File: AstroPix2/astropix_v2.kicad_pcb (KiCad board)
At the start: 4 copper layers, 51.3 x 48.8 mm, 45 parts, among them J1 pcie_GECCO, J10 SPI_right, J3 Vtemp1, J4 SFOut, J5 sample_clock_out, J6 HV_in_external, J8 VBias, J9 SPI_left, U1 TLV333, U2 SN65LVDS4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

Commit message: PCB: Small corrections
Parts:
- removed J8: VBias, Connector_PinHeader_2.54mm:PinHeader_1x03_P2.54mm_Vertical
- moved C11 3.20 mm to (120.8, 96.1)
- moved C14 3.17 mm to (117.6, 96.1)
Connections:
- U4 pad B24: /VPBias -> (no net)
- U4 pad B25: /pamp -> (no net)

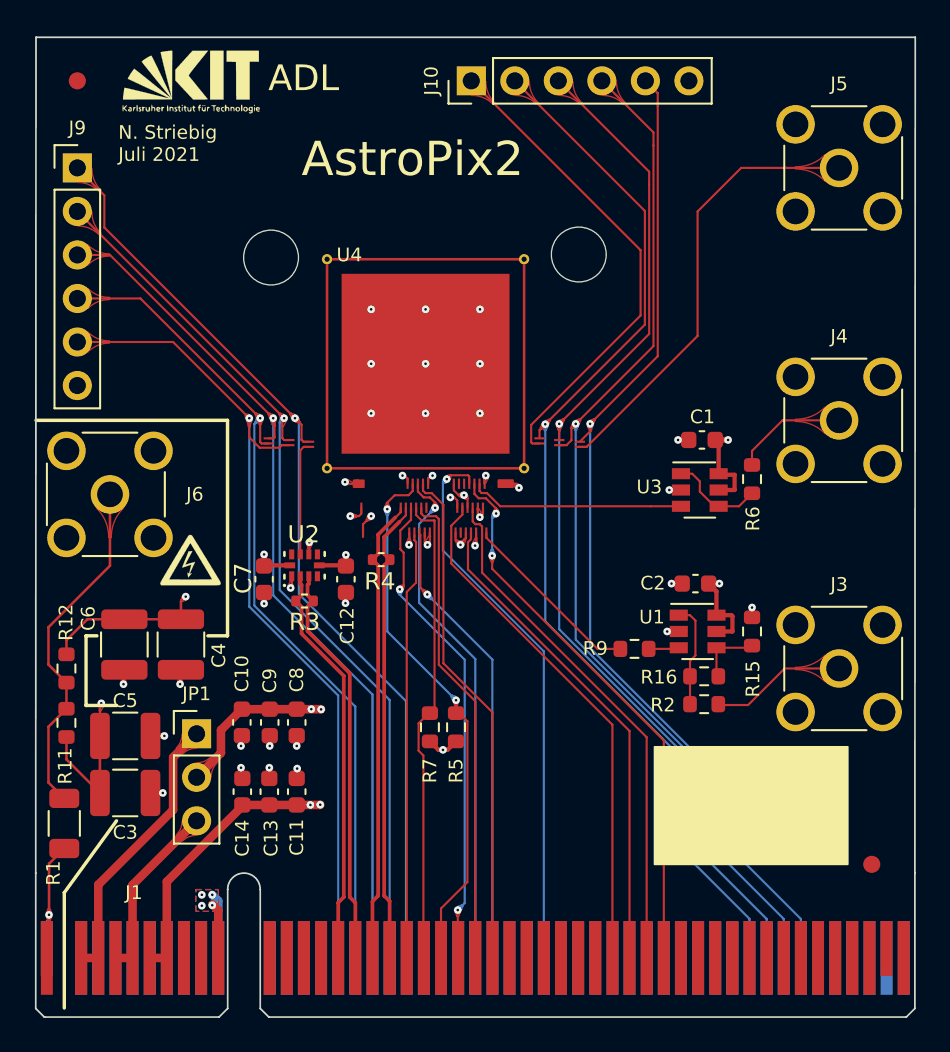
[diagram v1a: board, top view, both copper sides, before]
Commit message: PCB: Apix v2 updates
- Added SPI series resistors
- connected spi_right_clk to FMC
- Updated Amplifier Layout
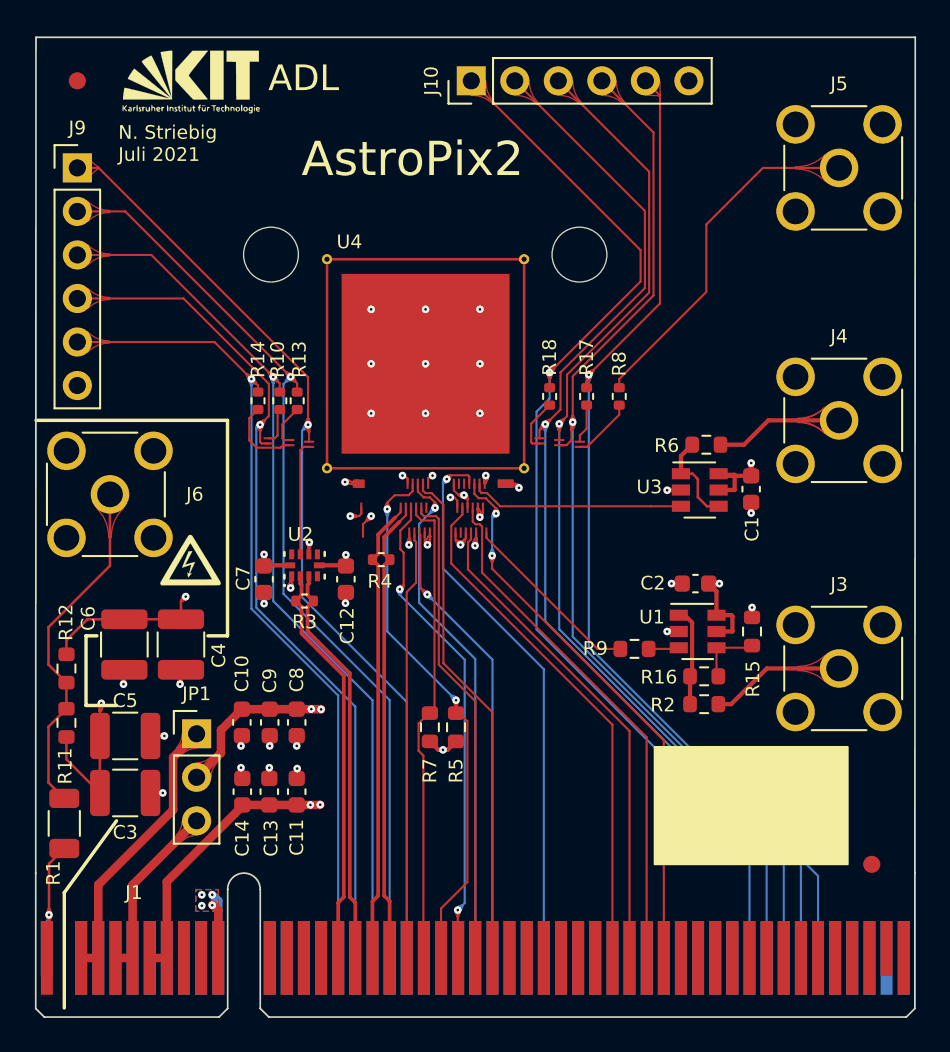
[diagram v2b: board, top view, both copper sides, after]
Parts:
- added R10: 22, Resistor_SMD:R_0402_1005Metric, F.Cu at (119.8, 73.3)
- added R13: 22, Resistor_SMD:R_0402_1005Metric, F.Cu at (120.8, 73.3)
- added R14: 22, Resistor_SMD:R_0402_1005Metric, F.Cu at (118.5, 73.3)
- added R17: 22, Resistor_SMD:R_0402_1005Metric, F.Cu at (137.7, 73.0)
- added R18: 22, Resistor_SMD:R_0402_1005Metric, F.Cu at (135.5, 73.0)
- added R8: 22, Resistor_SMD:R_0402_1005Metric, F.Cu at (139.6, 73.0)
- R6: value 22 -> 47
- moved C1 4.06 mm to (147.3, 78.4), turned to 270 degrees
- moved R6 3.34 mm to (144.7, 75.8), turned to 180 degrees
- moved H1 0.17 mm to (119.2, 64.8)
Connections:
- J1 pad A40: /spi_right_miso1 -> /spi_right_clk
- J1 pad A41: /spi_right_miso0 -> /spi_right_miso1
- J1 pad A42: /spi_right_csn -> /spi_right_miso0
- J1 pad A43: /spi_right_mosi -> /spi_right_csn
- J1 pad A44: (no net) -> /spi_right_mosi
- U4 pad L1: /spi_left_miso1 -> Net-(R10-Pad1)
- U4 pad L2: /spi_left_miso0 -> Net-(R13-Pad1)
- U4 pad L5: /spi_left_csn -> Net-(R14-Pad1)
- U4 pad R1: /sc_out -> Net-(R8-Pad2)
- U4 pad R3: /spi_right_clk -> Net-(R18-Pad2)
- U4 pad R4: /spi_right_mosi -> Net-(R17-Pad2)
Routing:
- net /spi_right_clk: track 28.3 -> 63.8 mm, vias 0 -> 1
- net /sc_out: track 26.2 -> 20.7 mm
- net Net-(R14-Pad1): track 0.00 -> 4.59 mm
- net Net-(J4-Pad1): track 6.64 -> 10.8 mm
- net Net-(R8-Pad2): track 0.00 -> 3.64 mm
- net Net-(R18-Pad2): track 0.00 -> 3.13 mm
- net Net-(R13-Pad1): track 0.00 -> 2.48 mm
- net Net-(R17-Pad2): track 0.00 -> 2.30 mm
- net Net-(R10-Pad1): track 0.00 -> 2.15 mm
- net /spi_left_csn: track 49.5 -> 47.9 mm
- net /spi_left_clk: track 49.6 -> 51.0 mm
- net /spi_left_miso0: track 53.0 -> 54.1 mm
- net /spi_left_miso1: track 50.8 -> 51.7 mm
- net /spi_right_csn: track 61.2 -> 61.8 mm

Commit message: PCB: Added holes for HIT bonding fixture
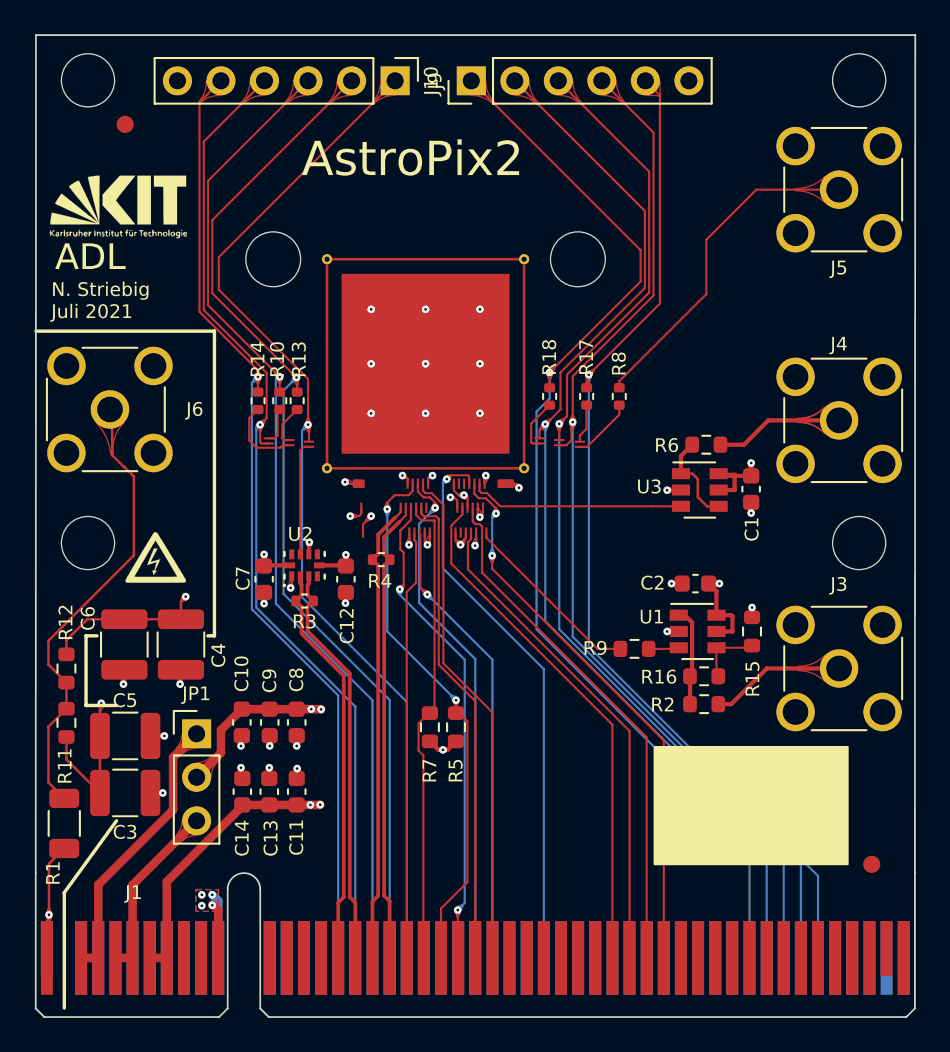
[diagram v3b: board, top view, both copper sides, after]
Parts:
- added H3: bonder, astropix:bonder, F.Cu at (131.6, 68.6)
- moved J9 19.2 mm to (126.5, 54.6), turned to 270 degrees
- moved Logo1 8.43 mm to (110.4, 62.0)
- moved J6 4.95 mm to (109.9, 73.8)
- moved FID1 3.78 mm to (110.7, 57.1)
- moved Logo2 2.04 mm to (112.5, 82.4)
- moved J5 1.27 mm to (152.4, 61.0)
- moved H1 0.30 mm to (119.4, 65.0)
- moved H2 0.29 mm to (137.2, 65.0)
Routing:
- net /spi_left_csn: track 47.9 -> 56.2 mm
- net /spi_left_clk: track 51.0 -> 58.4 mm
- net /spi_left_miso1: track 51.7 -> 58.6 mm
- net /spi_left_miso0: track 54.1 -> 60.3 mm
- net /HV_in_ext: track 20.5 -> 26.6 mm
- net /spi_left_mosi: track 56.1 -> 61.3 mm
- net /sc_out: track 20.7 -> 19.7 mm
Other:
- board size 51.3 x 48.8 mm -> 51.3 x 48.9 mm

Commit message: PCB V2: Connected SR_out/RB + Updated production files
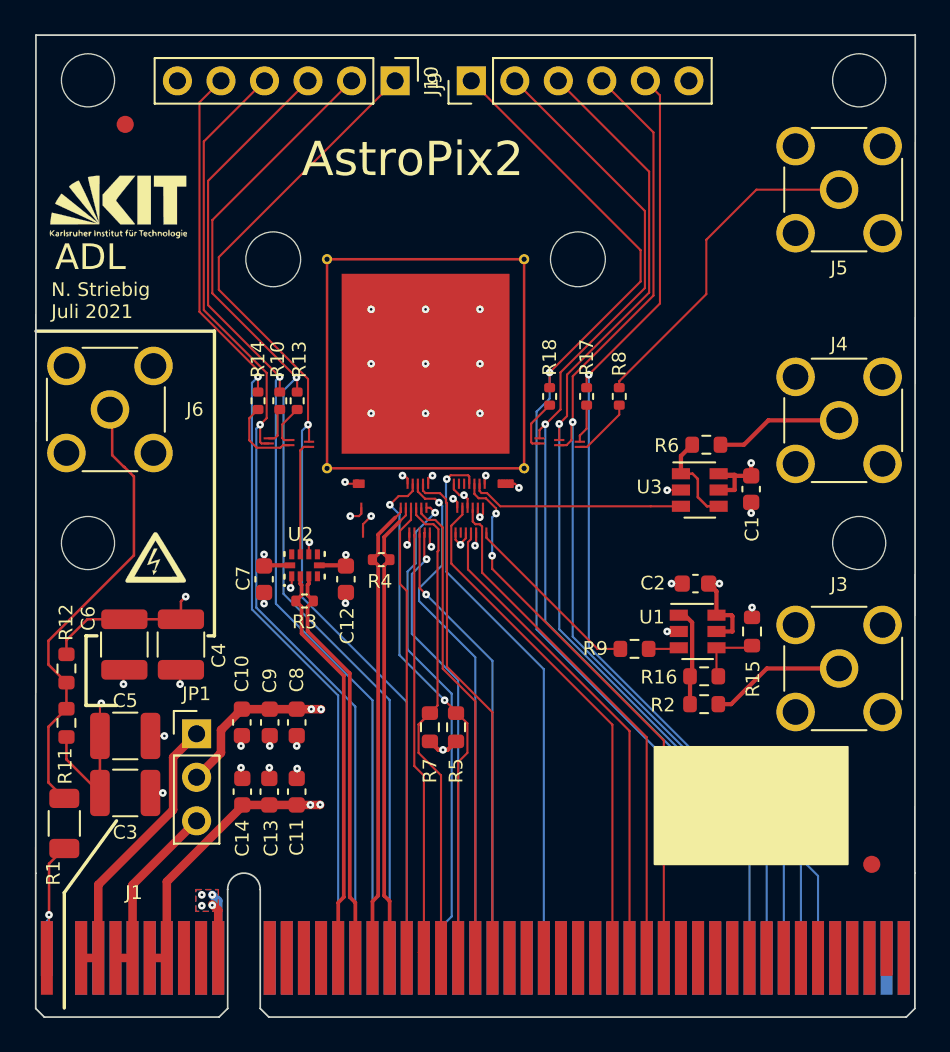
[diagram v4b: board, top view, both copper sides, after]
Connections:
- J1 pad A22: (no net) -> /sr_out
- J1 pad A23: (no net) -> /sr_rb
- J1 pad B20: /timestamp_clk -> /hold
- J1 pad B21: /interrupt -> /timestamp_clk
- J1 pad B22: /res_n -> /interrupt
- J1 pad B23: /hold -> /res_n
- U4 pad B17: GND -> /sr_rb
- U4 pad B18: (no net) -> /sr_out
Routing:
- net /sr_out: track 0.00 -> 28.6 mm, vias 0 -> 1
- net /sr_rb: track 0.00 -> 26.4 mm, vias 0 -> 1
- net /hold: track 28.5 -> 26.7 mm, vias 2 -> 0
- net /interrupt: track 27.7 -> 29.0 mm
- net GND: track 29.6 -> 28.7 mm
- net /res_n: track 31.4 -> 30.7 mm

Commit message: PCB V2: Updated Teardrops
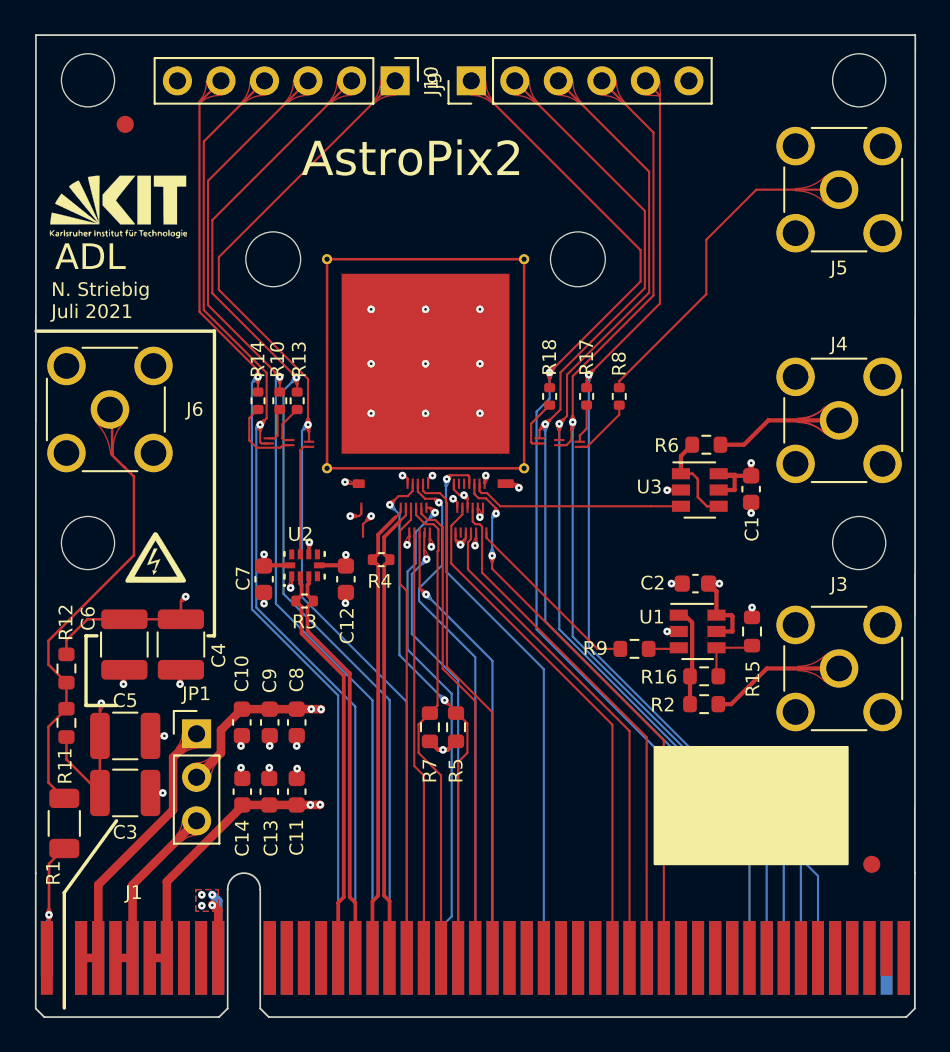
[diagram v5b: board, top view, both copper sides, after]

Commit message: PCB v2: Added markings for Bonding
-Updated gerber and assembly files
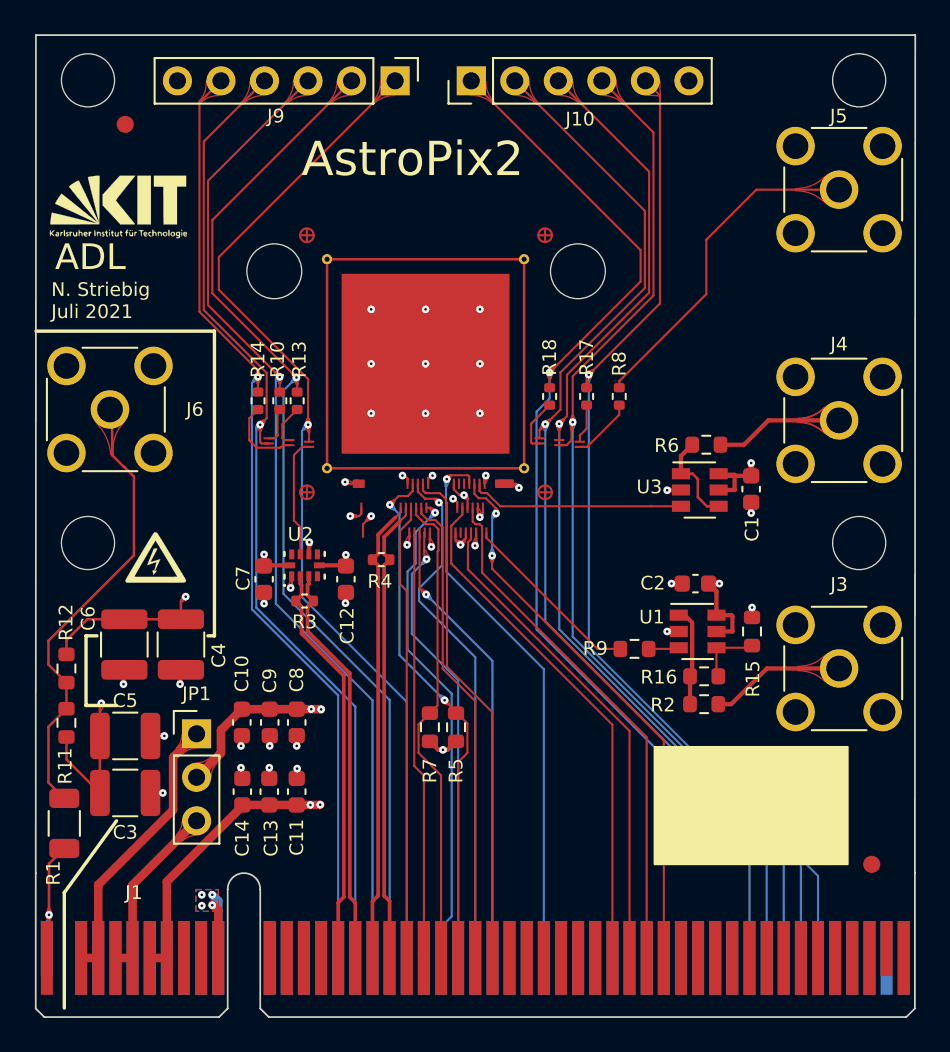
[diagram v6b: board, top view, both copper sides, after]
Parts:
- U4: footprint astropix:AstroPix2 -> astropix:AstroPix2_v2
- moved H1 0.70 mm to (119.4, 65.7)
- moved H2 0.70 mm to (137.2, 65.7)
